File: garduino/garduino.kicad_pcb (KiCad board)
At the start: 2 copper layers, 99.1 x 66.7 mm, 74 parts, among them J1 AIN0, J10 DIN1, J11 OUT6, J12 OUT5, J13 pgm, J14 OUT4, J15 OUT3, J16 OUT2, J17 OUT1, J18 RL0, J19 isp, J2 AIN1, J20 PWR, J3 AIN2, J4 AIN3, J5 AIN4, J6 I2C, J7 AIN4, J8 OUT7, J9 DIN0, Q1 Q_PNP_BCE, Q2 Q_PNP_BCE, Q3 Q_PNP_BCE, Q4 Q_PNP_BCE, Q5 Q_PNP_BCE, Q6 Q_PNP_BCE, Q7 Q_PNP_BCE, Q8 Q_PNP_BCE, SW1 reset, U1 TPIC6595, U2 ATmega168-20AU, U3 LM7805_TO220, U4 LM358, U5 LM358, U6 LM358, Y1 16MHz

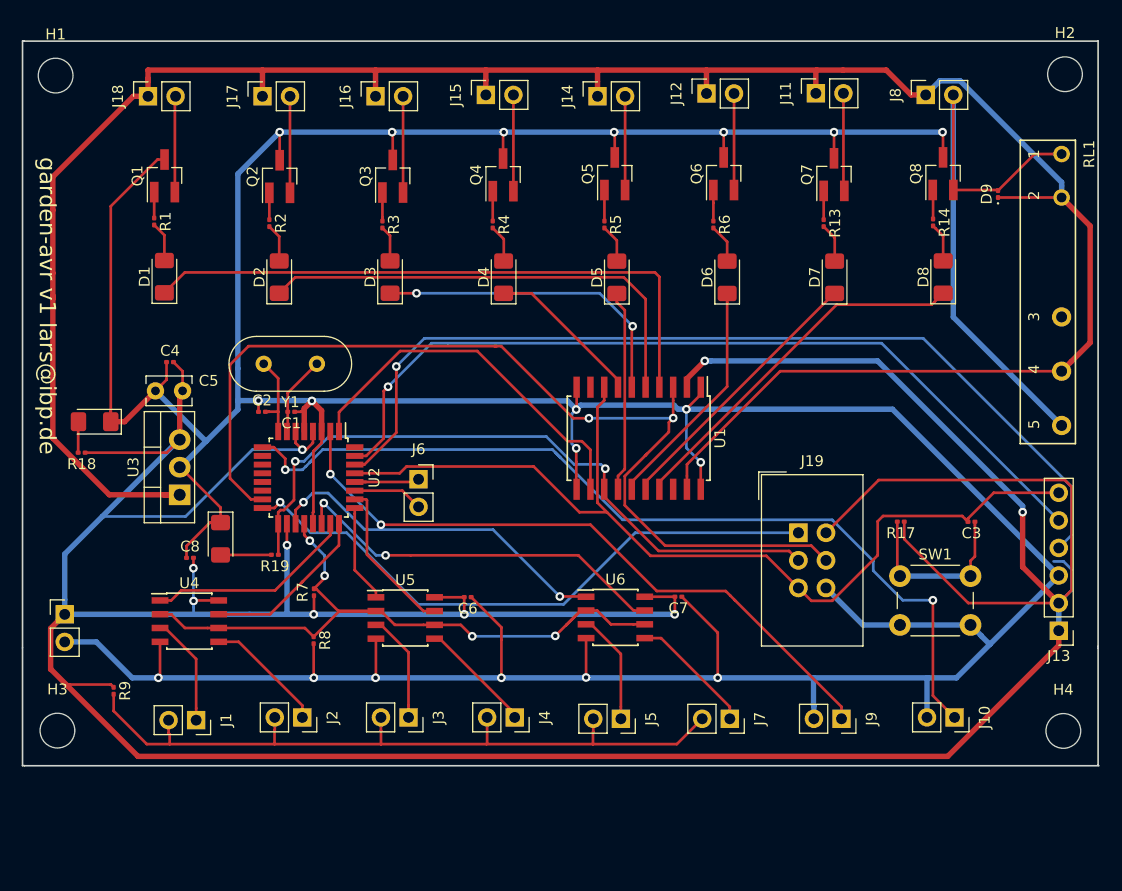
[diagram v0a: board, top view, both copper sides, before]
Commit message: Make garduino a Pi hat
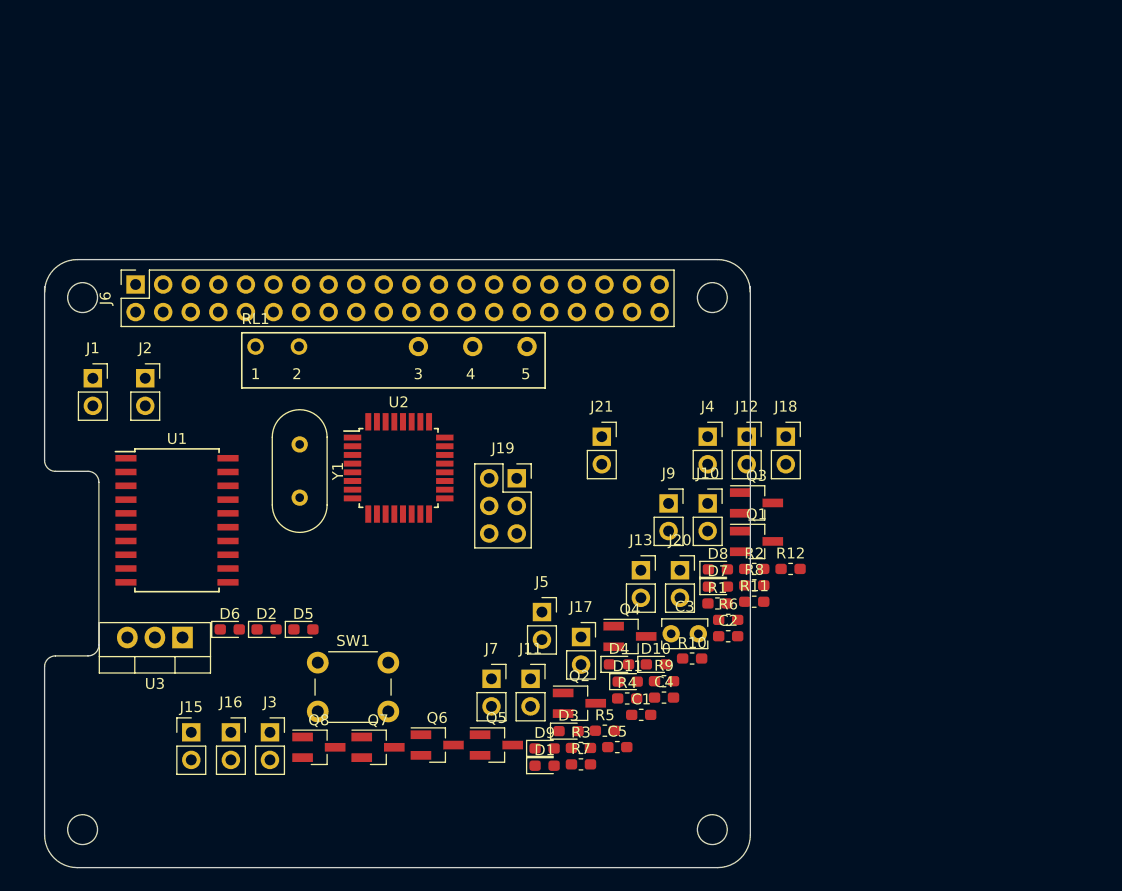
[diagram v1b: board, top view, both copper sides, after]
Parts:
- removed C6, C7, C8: 100nF, Capacitor_SMD:C_0201_0603Metric
- removed H1, H2, H3, H4: MountingHole, MountingHole:MountingHole_3.2mm_M3_DIN965
- removed J14: OUT4, Connector_PinSocket_2.54mm:PinSocket_1x02_P2.54mm_Vertical
- removed J8: OUT7, Connector_PinSocket_2.54mm:PinSocket_1x02_P2.54mm_Vertical
- removed R13, R14, R18, R19: 1k, Resistor_SMD:R_0201_0603Metric
- removed R17: 10k, Resistor_SMD:R_0201_0603Metric
- removed U4, U5, U6: LM358, Package_SO:SOIC-8_3.9x4.9mm_P1.27mm
- added ?: , RPi_Hat:RPi_Hat_Mounting_Hole, F.Cu at (151.2, 92.1)
- added ?: , RPi_Hat:RPi_Hat_Mounting_Hole, F.Cu at (151.2, 141.1)
- added ?: , RPi_Hat:RPi_Hat_Mounting_Hole, F.Cu at (93.2, 141.1)
- added ?: , RPi_Hat:RPi_Hat_Mounting_Hole, F.Cu at (93.2, 92.1)
- added J21: RL0, Connector_PinSocket_2.54mm:PinSocket_1x02_P2.54mm_Vertical, F.Cu at (141.0, 104.9)
- added R10: 10k, Resistor_SMD:R_0603_1608Metric_Pad1.05x0.95mm_HandSolder, F.Cu at (149.3, 125.4)
- added R11: 1k, Resistor_SMD:R_0603_1608Metric_Pad1.05x0.95mm_HandSolder, F.Cu at (155.0, 120.1)
- added R12: 1k, Resistor_SMD:R_0603_1608Metric_Pad1.05x0.95mm_HandSolder, F.Cu at (158.4, 117.1)
- C1, C2, C4: footprint Capacitor_SMD:C_0201_0603Metric -> Capacitor_SMD:C_0603_1608Metric_Pad1.05x0.95mm_HandSolder
- C3: value 100nF -> 1mF; footprint Capacitor_SMD:C_0201_0603Metric -> Capacitor_THT:C_Rect_L4.0mm_W2.5mm_P2.50mm
- C5: value 1mF -> 100nF; footprint Capacitor_THT:C_Rect_L4.0mm_W2.5mm_P2.50mm -> Capacitor_SMD:C_0603_1608Metric_Pad1.05x0.95mm_HandSolder
- D1, D10, D11, D2, D3, D4, D5, D6, D7, D8: footprint LED_SMD:LED_1206_3216Metric_Pad1.42x1.75mm_HandSolder -> LED_SMD:LED_0603_1608Metric_Pad1.05x0.95mm_HandSolder
- D9: footprint Diode_SMD:D_0201_0603Metric -> Diode_SMD:D_0603_1608Metric_Pad1.05x0.95mm_HandSolder
- J10: value DIN1 -> DIN0
- J11: value OUT6 -> DIN1
- J12: value OUT5 -> OUT6
- J13: value pgm -> OUT5; footprint Connector_PinHeader_2.54mm:PinHeader_1x06_P2.54mm_Vertical -> Connector_PinSocket_2.54mm:PinSocket_1x02_P2.54mm_Vertical
- J15: value OUT3 -> PWR; footprint Connector_PinSocket_2.54mm:PinSocket_1x02_P2.54mm_Vertical -> Connector_PinHeader_2.54mm:PinHeader_1x02_P2.54mm_Vertical
- J16: value OUT2 -> OUT4
- J17: value OUT1 -> OUT3
- J18: value RL0 -> OUT2
- J19: footprint Connector_IDC:IDC-Header_2x03_P2.54mm_Vertical -> Connector_PinSocket_2.54mm:PinSocket_2x03_P2.54mm_Vertical
- J20: value PWR -> OUT1; footprint Connector_PinHeader_2.54mm:PinHeader_1x02_P2.54mm_Vertical -> Connector_PinSocket_2.54mm:PinSocket_1x02_P2.54mm_Vertical
- J6: value I2C -> RPi; footprint Connector_PinSocket_2.54mm:PinSocket_1x02_P2.54mm_Vertical -> Connector_PinSocket_2.54mm:PinSocket_2x20_P2.54mm_Vertical
- J9: value DIN0 -> OUT7
- R1, R3: value 1k -> 10k; footprint Resistor_SMD:R_0201_0603Metric -> Resistor_SMD:R_0603_1608Metric_Pad1.05x0.95mm_HandSolder
- R2, R7, R8, R9: value 10k -> 1k; footprint Resistor_SMD:R_0201_0603Metric -> Resistor_SMD:R_0603_1608Metric_Pad1.05x0.95mm_HandSolder
- R4, R5, R6: footprint Resistor_SMD:R_0201_0603Metric -> Resistor_SMD:R_0603_1608Metric_Pad1.05x0.95mm_HandSolder
- moved Q8 78.1 mm to (114.9, 133.6), turned to 0 degrees
- moved RL1 76.3 mm to (109.1, 96.6), turned to 0 degrees
- moved Q7 67.4 mm to (120.4, 133.6), turned to 0 degrees
- moved J18 66.6 mm to (157.9, 104.9), turned to 0 degrees
- moved D9 66.0 mm to (135.7, 133.7), turned to 0 degrees
- moved J15 64.7 mm to (103.2, 132.2), turned to 0 degrees
- moved Q1 64.1 mm to (155.2, 114.6), turned to 0 degrees
- moved R1 62.7 mm to (151.6, 120.3), turned to 0 degrees
- moved J16 60.1 mm to (106.8, 132.2), turned to 0 degrees
- moved J11 60.0 mm to (134.4, 127.2), turned to 0 degrees
- moved Q6 58.9 mm to (125.8, 133.3), turned to 0 degrees
- moved J17 57.8 mm to (139.1, 123.4), turned to 0 degrees
- moved D1 57.1 mm to (135.7, 135.2), turned to 0 degrees
- moved J20 56.8 mm to (148.2, 117.2)
- moved D10 56.3 mm to (146.0, 125.9), turned to 0 degrees
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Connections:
- C3 pad 1: Net-(C3-Pad1) -> GND
- C3 pad 2: /RTS# -> +5V
- C5 pad 1: GND -> Net-(C5-Pad1)
- C5 pad 2: +5V -> /RTS#
- J1 pad 1: /AIN0 -> (no net)
- J10 pad 1: /PD5 -> /PD4
- J11 pad 1: +12V -> /PD5
- J11 pad 2: /OUT6 -> GND
- J12 pad 2: /OUT5 -> /OUT6
- J13 pad 1: +5V -> +12V
- J13 pad 2: +5V -> /OUT5
- J15 pad 1: +12V -> +5V
- J15 pad 2: /OUT3 -> GND
- J16 pad 2: /OUT2 -> /OUT4
- J17 pad 2: /OUT1 -> /OUT3
- J18 pad 2: /OUT0 -> /OUT2
- J2 pad 1: /AIN1 -> (no net)
- J20 pad 1: +5V -> +12V
- J20 pad 2: GND -> /OUT1
- J3 pad 1: /AIN2 -> (no net)
- J4 pad 1: /AIN3 -> (no net)
- J5 pad 1: /AIN4 -> (no net)
- J6 pad 1: /SDA -> (no net)
- J6 pad 2: /SCL -> /5v
- J7 pad 1: /AIN5 -> (no net)
- J9 pad 1: /PD4 -> +12V
- J9 pad 2: GND -> /RL0
- R1 pad 1: Net-(Q1-Pad1) -> +5V
- R1 pad 2: Net-(D1-Pad2) -> Net-(J1-Pad2)
- R2 pad 1: Net-(Q2-Pad1) -> Net-(Q1-Pad1)
- R2 pad 2: Net-(D2-Pad2) -> Net-(D1-Pad2)
- R3 pad 1: Net-(Q3-Pad1) -> Net-(Q2-Pad1)
- R3 pad 2: Net-(D3-Pad2) -> Net-(D2-Pad2)
- R4 pad 1: Net-(Q4-Pad1) -> Net-(Q3-Pad1)
- R4 pad 2: Net-(D4-Pad2) -> Net-(D3-Pad2)
- R5 pad 1: Net-(Q5-Pad1) -> Net-(Q4-Pad1)
- R5 pad 2: Net-(D5-Pad2) -> Net-(D4-Pad2)
- R6 pad 1: Net-(Q6-Pad1) -> Net-(Q5-Pad1)
- R6 pad 2: Net-(D6-Pad2) -> Net-(D5-Pad2)
- R7 pad 1: +5V -> Net-(Q6-Pad1)
- R7 pad 2: /AREF -> Net-(D6-Pad2)
- R8 pad 1: /AREF -> Net-(Q7-Pad1)
- R8 pad 2: GND -> Net-(D7-Pad2)
- R9 pad 1: +5V -> Net-(Q8-Pad1)
- R9 pad 2: Net-(J1-Pad2) -> Net-(D8-Pad2)
- RL1 pad 3: Net-(RL1-Pad3) -> (no net)
- SW1 pad 1: Net-(C3-Pad1) -> Net-(C5-Pad1)
- U1 pad 18: Net-(U1-Pad18) -> (no net)
- U1 pad 9: /G# -> (no net)
- U2 pad 10: Net-(U2-Pad10) -> (no net)
- U2 pad 11: Net-(U2-Pad11) -> (no net)
- U2 pad 12: Net-(U2-Pad12) -> (no net)
- U2 pad 13: Net-(U2-Pad13) -> (no net)
- U2 pad 14: Net-(U2-Pad14) -> (no net)
- U2 pad 19: /ADC6 -> (no net)
- U2 pad 20: /AREF -> (no net)
- U2 pad 21: GND -> Net-(U2-Pad21)
- U2 pad 22: /ADC7 -> (no net)
- U2 pad 23: /PC0 -> (no net)
- U2 pad 24: /PC1 -> (no net)
- U2 pad 25: /PC2 -> (no net)
- U2 pad 26: /PC3 -> (no net)
- U2 pad 27: /SCL -> (no net)
- U2 pad 28: /SDA -> (no net)
- U2 pad 3: GND -> Net-(U2-Pad21)
- U2 pad 30: Net-(J13-Pad4) -> /PITX0
- U2 pad 31: Net-(J13-Pad5) -> /PIRX0
- U2 pad 32: /G -> (no net)
- U2 pad 5: GND -> Net-(U2-Pad21)
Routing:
- net GND: track 440.0 -> 0.00 mm, vias 19 -> 0
- net +5V: track 368.3 -> 0.00 mm, vias 9 -> 0
- net +12V: track 223.1 -> 0.00 mm
- net /MOSI: track 91.9 -> 0.00 mm, vias 2 -> 0
- net /RTS#: track 88.9 -> 0.00 mm
- net Net-(J13-Pad4): track 86.2 -> 0.00 mm, vias 1 -> 0
- net /PD5: track 84.1 -> 0.00 mm, vias 2 -> 0
- net Net-(J13-Pad5): track 78.4 -> 0.00 mm, vias 1 -> 0
- net Net-(J1-Pad2): track 70.0 -> 0.00 mm
- net /AREF: track 65.1 -> 0.00 mm, vias 4 -> 0
- net /SCK: track 63.1 -> 0.00 mm, vias 2 -> 0
- net /PD4: track 61.0 -> 0.00 mm, vias 2 -> 0
- net /DRAIN0: track 56.7 -> 0.00 mm
- net /MISO: track 56.2 -> 0.00 mm, vias 1 -> 0
- net /DRAIN1: track 43.3 -> 0.00 mm
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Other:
- board size 99.1 x 66.7 mm -> 65 x 56 mm
- net class Default: via_dia 0.8 -> 0.6
- rule pad_to_mask_clearance: 0.051 -> 0
- rule trace_min: 0.2 -> 0.01
- board text added: "Camera Flex Slot (Optional)"
- board text added: "Dimensions taken from https://github.com/raspberrypi/hats/blob/master/hat-board-mechanical.pdf"
- board text added: "Select one of these board edges depending upon the type of socket that is used."
- board text removed: "garden-avr v1 lars@ibp.de"

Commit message: Schematic and PCB for Pluto mute circuit
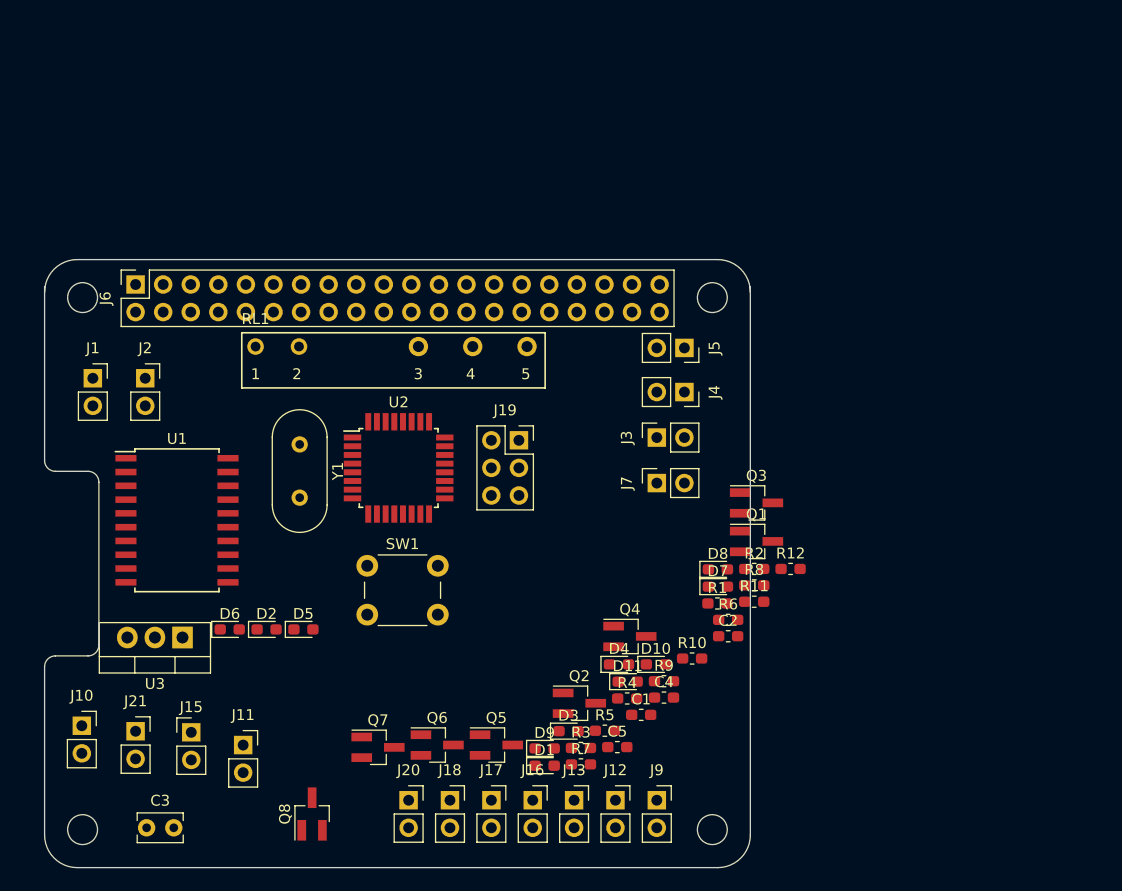
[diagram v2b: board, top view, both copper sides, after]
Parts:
- moved J10 61.2 mm to (93.1, 131.6)
- moved C3 51.5 mm to (99.1, 141.0)
- moved J21 50.8 mm to (98.0, 132.1)
- moved J18 45.6 mm to (127.0, 138.4)
- moved J3 44.8 mm to (146.1, 105.0), turned to 90 degrees
- moved J12 35.6 mm to (142.2, 138.4)
- moved J20 32.8 mm to (123.2, 138.4)
- moved J16 28.5 mm to (134.6, 138.4)
- moved J5 27.6 mm to (148.6, 96.8), turned to 270 degrees
- moved J9 27.4 mm to (146.1, 138.4)
- moved J11 27.2 mm to (108.0, 133.3)
- moved J7 23.6 mm to (146.1, 109.2), turned to 90 degrees
- moved J13 22.1 mm to (138.4, 138.4)
- moved J17 17.2 mm to (130.8, 138.4)
- moved SW1 10.0 mm to (119.4, 116.8)
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
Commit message: garduino WIP
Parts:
- removed C4, C5: 100nF, Capacitor_SMD:C_0603_1608Metric_Pad1.05x0.95mm_HandSolder
- removed J19: isp, Connector_PinSocket_2.54mm:PinSocket_2x03_P2.54mm_Vertical
- removed J20: OUT1, Connector_PinSocket_2.54mm:PinSocket_1x02_P2.54mm_Vertical
- removed J21: RL0, Connector_PinSocket_2.54mm:PinSocket_1x02_P2.54mm_Vertical
- removed R12: 1k, Resistor_SMD:R_0603_1608Metric_Pad1.05x0.95mm_HandSolder
- removed Y1: 16MHz, Crystal:Crystal_HC18-U_Vertical
- added D13: LED, LED_SMD:LED_0603_1608Metric_Pad1.05x0.95mm_HandSolder, F.Cu at (147.7, 97.8)
- added J14: OUT3, Connector_PinSocket_2.54mm:PinSocket_1x02_P2.54mm_Vertical, F.Cu at (113.0, 142.2)
- added J8: OUT7, Connector_PinSocket_2.54mm:PinSocket_1x02_P2.54mm_Vertical, F.Cu at (142.2, 142.2)
- added R13: 1k, Resistor_SMD:R_0603_1608Metric_Pad1.05x0.95mm_HandSolder, F.Cu at (143.9, 97.8)
- C1: value 22pF -> 1mF; footprint Capacitor_SMD:C_0603_1608Metric_Pad1.05x0.95mm_HandSolder -> Capacitor_THT:C_Rect_L4.0mm_W2.5mm_P2.50mm
- C2: value 22pF -> 100nF
- C3: value 1mF -> 100nF; footprint Capacitor_THT:C_Rect_L4.0mm_W2.5mm_P2.50mm -> Capacitor_SMD:C_0603_1608Metric_Pad1.05x0.95mm_HandSolder
- J1: value AIN0 -> Hum1; footprint Connector_PinSocket_2.54mm:PinSocket_1x02_P2.54mm_Vertical -> Connector_PinHeader_2.54mm:PinHeader_1x04_P2.54mm_Vertical
- J10: value DIN0 -> OUT6
- J12: value OUT6 -> OUT5
- J13: value OUT5 -> OUT4
- J15: value PWR -> isp; footprint Connector_PinHeader_2.54mm:PinHeader_1x02_P2.54mm_Vertical -> Connector_PinSocket_2.54mm:PinSocket_2x03_P2.54mm_Vertical
- J16: value OUT4 -> OUT2
- J17: value OUT3 -> OUT1
- J18: value OUT2 -> RPi; footprint Connector_PinSocket_2.54mm:PinSocket_1x02_P2.54mm_Vertical -> Connector_PinSocket_2.54mm:PinSocket_2x20_P2.54mm_Vertical
- J2: value AIN1 -> Hum2; footprint Connector_PinSocket_2.54mm:PinSocket_1x02_P2.54mm_Vertical -> Connector_PinHeader_2.54mm:PinHeader_1x04_P2.54mm_Vertical
- J3: value AIN2 -> Hum3; footprint Connector_PinSocket_2.54mm:PinSocket_1x02_P2.54mm_Vertical -> Connector_PinHeader_2.54mm:PinHeader_1x04_P2.54mm_Vertical
- J4: value AIN3 -> Hum4; footprint Connector_PinSocket_2.54mm:PinSocket_1x02_P2.54mm_Vertical -> Connector_PinHeader_2.54mm:PinHeader_1x04_P2.54mm_Vertical
- J5: value AIN4 -> Hum5; footprint Connector_PinSocket_2.54mm:PinSocket_1x02_P2.54mm_Vertical -> Connector_PinHeader_2.54mm:PinHeader_1x04_P2.54mm_Vertical
- J6: value RPi -> Hum6; footprint Connector_PinSocket_2.54mm:PinSocket_2x20_P2.54mm_Vertical -> Connector_PinHeader_2.54mm:PinHeader_1x04_P2.54mm_Vertical
- J7: value AIN4 -> RL0
- J9: value OUT7 -> DIN0
- R1, R10, R3: value 10k -> 1k
- R2, R9: value 1k -> 10k
- U2: value ATmega168-20AU -> ATmega328-AU
- moved Q1 60.1 mm to (98.0, 133.0)
- moved J2 59.5 mm to (152.1, 126.2)
- moved R2 59.1 mm to (97.2, 128.9), turned to 90 degrees
- moved J6 58.3 mm to (152.1, 112.5), turned to 0 degrees
- moved J4 56.7 mm to (91.9, 97.8), turned to 0 degrees
- moved J18 55.3 mm to (97.8, 91.4), turned to 90 degrees
- moved J5 54.3 mm to (97.5, 115.3), turned to 0 degrees
- moved R1 53.9 mm to (98.0, 126.2)
- moved D8 51.2 mm to (101.1, 109.0), turned to 90 degrees
- moved R9 49.4 mm to (105.4, 100.3)
- moved Q3 47.4 mm to (113.3, 133.0)
- moved D9 45.1 mm to (102.1, 103.6), turned to 180 degrees
- moved U3 44.7 mm to (144.8, 109.2), turned to 270 degrees
- moved J10 42.9 mm to (134.6, 142.2), turned to 90 degrees
- moved Q8 42.7 mm to (100.1, 99.4), turned to 180 degrees
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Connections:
- C1 pad 2: Net-(C1-Pad2) -> +5V
- C2 pad 2: Net-(C2-Pad2) -> +5V
- C3 pad 1: GND -> Net-(C3-Pad1)
- C3 pad 2: +5V -> /RESET
- J1 pad 1: (no net) -> +5V
- J1 pad 2: Net-(J1-Pad2) -> GND
- J10 pad 1: /PD4 -> +12V
- J10 pad 2: GND -> /OUT5
- J11 pad 1: /PD5 -> (no net)
- J12 pad 2: /OUT6 -> /OUT4
- J13 pad 2: /OUT5 -> /OUT3
- J15 pad 1: +5V -> /MISO
- J15 pad 2: GND -> +5V
- J16 pad 2: /OUT4 -> /OUT1
- J17 pad 2: /OUT3 -> /OUT0
- J18 pad 1: +12V -> (no net)
- J18 pad 2: /OUT2 -> /5v
- J2 pad 1: (no net) -> +5V
- J2 pad 2: Net-(J1-Pad2) -> (no net)
- J3 pad 1: (no net) -> +5V
- J3 pad 2: Net-(J1-Pad2) -> GND
- J4 pad 1: (no net) -> +5V
- J4 pad 2: Net-(J1-Pad2) -> GND
- J5 pad 1: (no net) -> +5V
- J5 pad 2: Net-(J1-Pad2) -> GND
- J6 pad 1: (no net) -> +5V
- J6 pad 2: /5v -> GND
- J6 pad 3: (no net) -> /SDA
- J6 pad 4: /5v -> /SCL
- J7 pad 1: (no net) -> +12V
- J7 pad 2: Net-(J1-Pad2) -> /RL0
- J9 pad 1: +12V -> (no net)
- J9 pad 2: /RL0 -> GND
- R1 pad 1: +5V -> Net-(Q1-Pad1)
- R1 pad 2: Net-(J1-Pad2) -> Net-(D1-Pad2)
- R10 pad 1: +5V -> /LED1
- R10 pad 2: Net-(C5-Pad1) -> Net-(D10-Pad2)
- R11 pad 1: +5V -> /LED2
- R11 pad 2: Net-(D10-Pad2) -> Net-(D11-Pad2)
- R2 pad 1: Net-(Q1-Pad1) -> Net-(Q2-Pad1)
- R2 pad 2: Net-(D1-Pad2) -> Net-(D2-Pad2)
- R3 pad 1: Net-(Q2-Pad1) -> Net-(Q3-Pad1)
- R3 pad 2: Net-(D2-Pad2) -> Net-(D3-Pad2)
- R4 pad 1: Net-(Q3-Pad1) -> Net-(Q4-Pad1)
- R4 pad 2: Net-(D3-Pad2) -> Net-(D4-Pad2)
- R5 pad 1: Net-(Q4-Pad1) -> Net-(Q5-Pad1)
- R5 pad 2: Net-(D4-Pad2) -> Net-(D5-Pad2)
- R6 pad 1: Net-(Q5-Pad1) -> Net-(Q6-Pad1)
- R6 pad 2: Net-(D5-Pad2) -> Net-(D6-Pad2)
- R7 pad 1: Net-(Q6-Pad1) -> Net-(Q7-Pad1)
- R7 pad 2: Net-(D6-Pad2) -> Net-(D7-Pad2)
- R8 pad 1: Net-(Q7-Pad1) -> Net-(Q8-Pad1)
- R8 pad 2: Net-(D7-Pad2) -> Net-(D8-Pad2)
- R9 pad 1: Net-(Q8-Pad1) -> +5V
- R9 pad 2: Net-(D8-Pad2) -> Net-(C3-Pad1)
- SW1 pad 1: Net-(C5-Pad1) -> Net-(C3-Pad1)
- U1 pad 8: /RTS# -> /RESET
- U1 pad 9: (no net) -> /G#
- U2 pad 1: /RCLK -> (no net)
- U2 pad 13: (no net) -> /RCLK
- U2 pad 14: (no net) -> /G#
- U2 pad 18: +5V -> (no net)
- U2 pad 2: /PD4 -> (no net)
- U2 pad 23: (no net) -> /LED1
- U2 pad 24: (no net) -> /LED2
- U2 pad 27: (no net) -> /SDA
- U2 pad 28: (no net) -> /SCL
- U2 pad 29: /RTS# -> /RESET
- U2 pad 30: /PITX0 -> (no net)
- U2 pad 31: /PIRX0 -> (no net)
- U2 pad 4: +5V -> Net-(U2-Pad4)
- U2 pad 6: +5V -> Net-(U2-Pad4)
- U2 pad 7: Net-(C1-Pad2) -> (no net)
- U2 pad 8: Net-(C2-Pad2) -> (no net)
- U2 pad 9: /PD5 -> (no net)
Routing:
- net /SCK: track 0.00 -> 131.4 mm, vias 0 -> 1
- net +12V: track 0.00 -> 130.4 mm, vias 0 -> 2
- net +5V: track 0.00 -> 100.0 mm
- net GND: track 0.00 -> 89.6 mm
- net /SDA: track 0.00 -> 58.0 mm, vias 0 -> 1
- net /MOSI: track 0.00 -> 42.9 mm
- net /DRAIN6: track 0.00 -> 41.3 mm
- net /SCL: track 0.00 -> 32.8 mm
- net /DRAIN5: track 0.00 -> 32.8 mm
- net /DRAIN3: track 0.00 -> 28.4 mm
- net /DRAIN4: track 0.00 -> 24.5 mm
- net /DRAIN2: track 0.00 -> 22.8 mm
- net Net-(C3-Pad1): track 0.00 -> 20.2 mm
- net /DRAIN0: track 0.00 -> 19.4 mm
- net /DRAIN1: track 0.00 -> 19.2 mm
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- added copper zone on B.Cu, net GND
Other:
- board text removed: "Dimensions taken from https://github.com/raspberrypi/hats/blob/master/hat-board-mechanical.pdf"
